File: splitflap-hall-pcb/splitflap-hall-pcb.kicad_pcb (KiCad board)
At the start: 2 copper layers, 13 x 20 mm, 5 parts, among them J1 640457-3, U1 AH1806-W

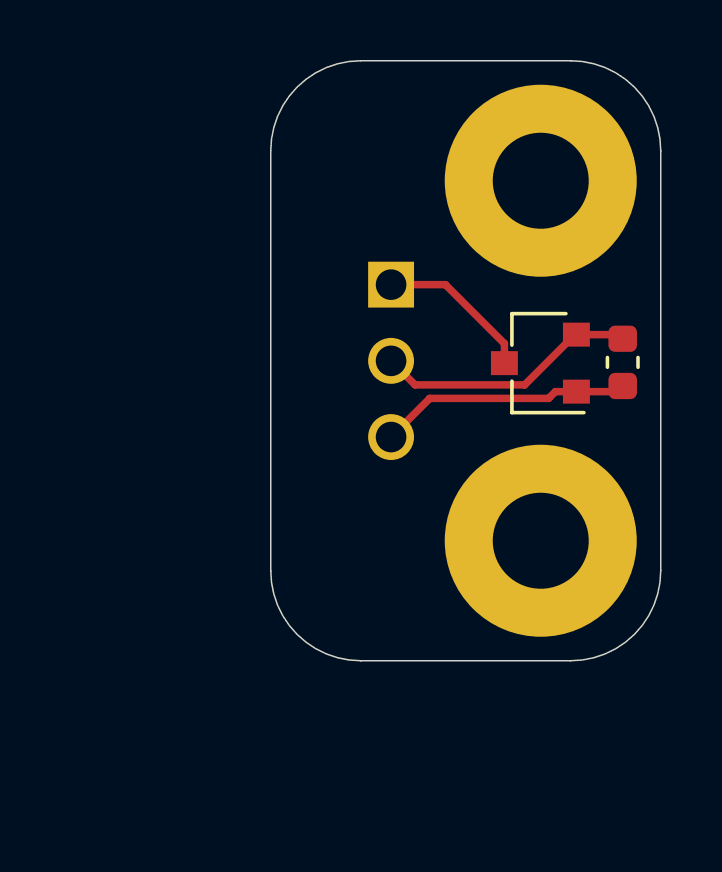
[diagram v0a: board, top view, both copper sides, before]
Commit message: Rotate SFH 90 degrees
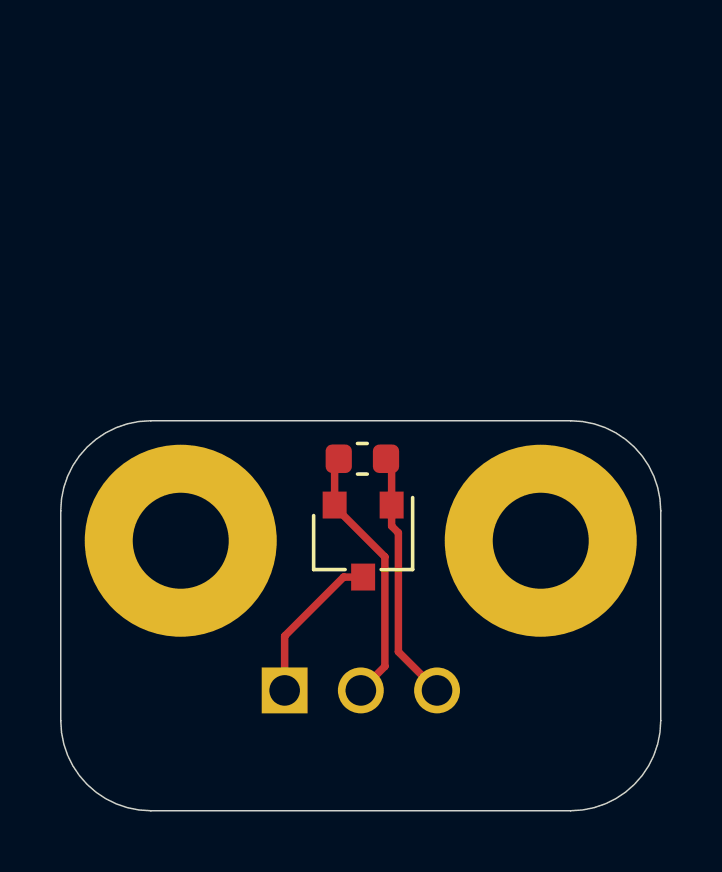
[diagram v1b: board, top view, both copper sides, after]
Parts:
- moved H1 17.0 mm to (81.0, 84.0), turned to 90 degrees
- moved J1 14.0 mm to (84.5, 89.0), turned to 180 degrees
- moved C1 9.25 mm to (87.1, 81.3), turned to 180 degrees
- moved U1 8.37 mm to (87.1, 84.0), turned to 270 degrees
- turned H2 to 90 degrees
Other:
- board size 13 x 20 mm -> 20 x 13 mm
